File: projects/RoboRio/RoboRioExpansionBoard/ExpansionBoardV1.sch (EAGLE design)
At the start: 78 parts, among them Q1 5MHz

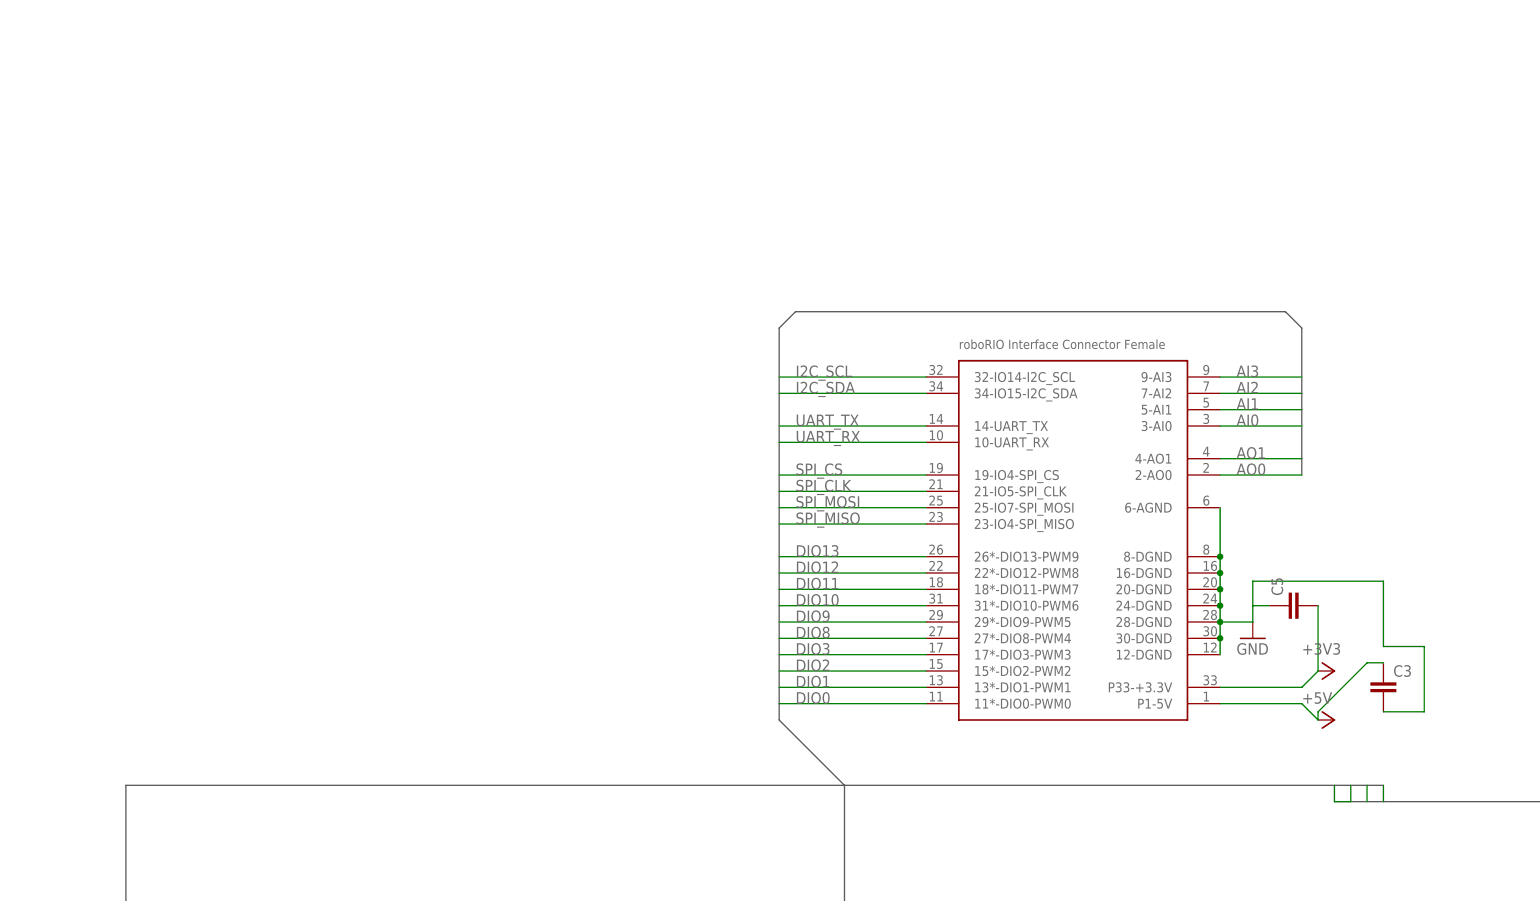
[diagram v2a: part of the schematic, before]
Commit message: AIO has been broken out
-Eric
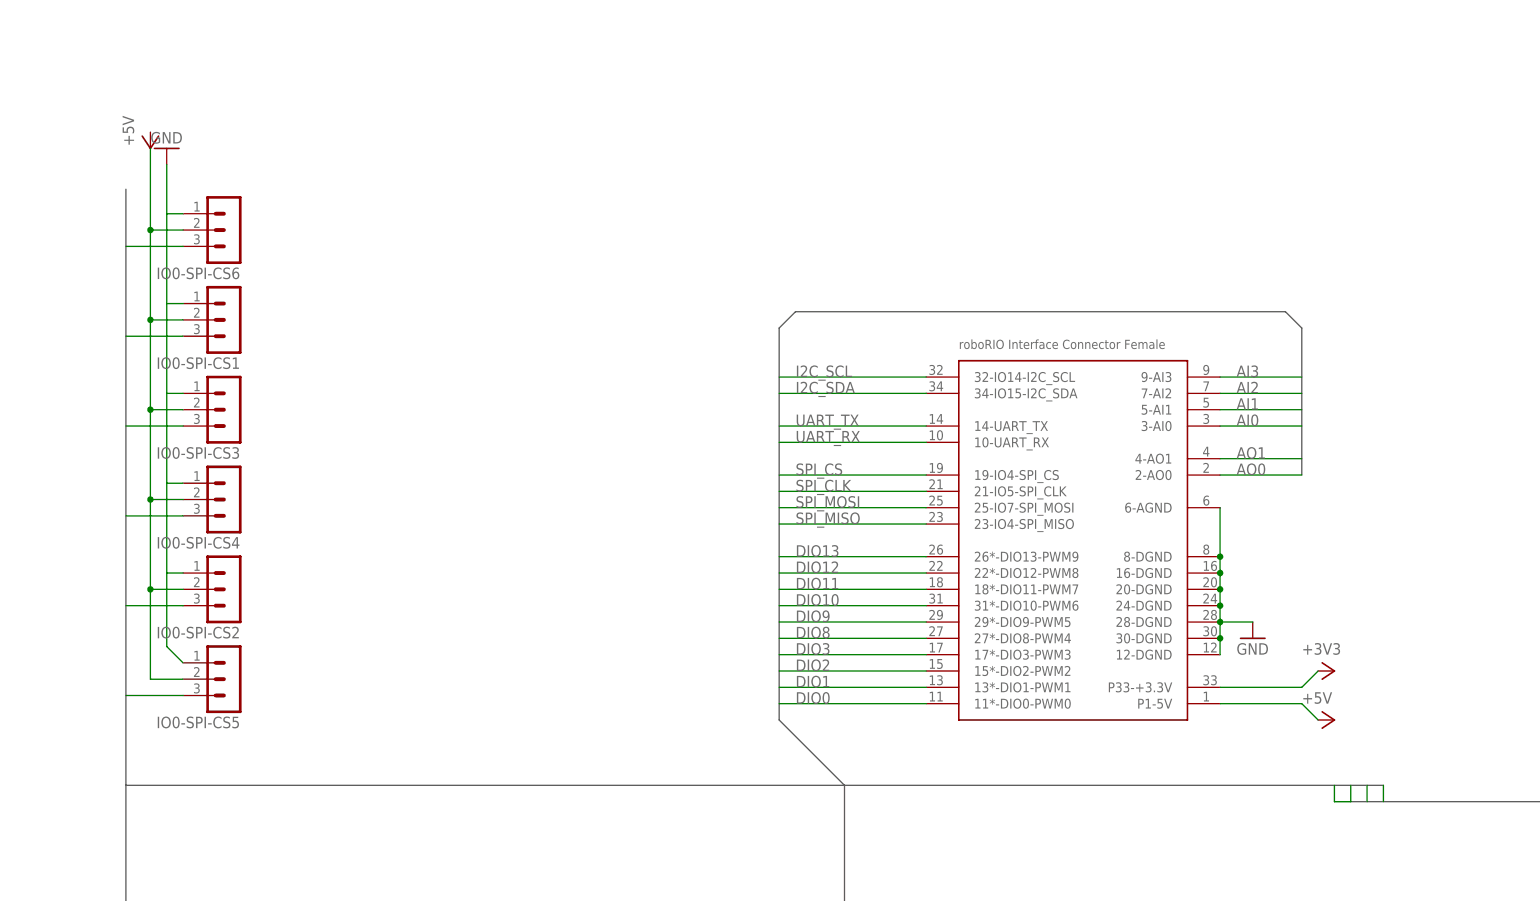
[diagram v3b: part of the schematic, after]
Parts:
- removed C3, C5: (no value), capacitor-wima:C7.5/6
- added IO0-SPI-CS1, IO0-SPI-CS2, IO0-SPI-CS3, IO0-SPI-CS4, IO0-SPI-CS5, IO0-SPI-CS6: (no value), con-lstb-modified:MA03-1
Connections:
- new net N$18: IO0-SPI-CS1.2, IO0-SPI-CS2.2, IO0-SPI-CS3.2, IO0-SPI-CS4.2, IO0-SPI-CS5.2, IO0-SPI-CS6.2
- net +3V3: no longer C5.2
- net +5V: no longer C3.1
- net AI0: now also IO0-SPI-CS6.3
- net AI1: now also IO0-SPI-CS1.3
- net AI2: now also IO0-SPI-CS3.3
- net AI3: now also IO0-SPI-CS4.3
- net AO0: now also IO0-SPI-CS2.3
- net AO1: now also IO0-SPI-CS5.3
- net GND: now also IO0-SPI-CS1.1, IO0-SPI-CS2.1, IO0-SPI-CS3.1, IO0-SPI-CS4.1, IO0-SPI-CS5.1, IO0-SPI-CS6.1; no longer C3.2, C5.1
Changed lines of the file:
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@@
 <part name="GND23" library="supply1" deviceset="GND" device=""/>
 <part name="C4" library="capacitor-wima" deviceset="C" device="7.5/6"/>
-<part name="C5" library="capacitor-wima" deviceset="C" device="7.5/6"/>
 <part name="C2" library="capacitor-wima" deviceset="C" device="7.5/6"/>
-<part name="C3" library="capacitor-wima" deviceset="C" device="7.5/6"/>
 <part name="C10" library="capacitor-wima" deviceset="C" device="7.5/6"/>
 <part name="C12" library="capacitor-wima" deviceset="C" device="7.5/6"/>
@@
 <part name="GND24" library="supply1" deviceset="GND" device=""/>
 <part name="R5" library="resistor" deviceset="R-US_" device="0309/V" value="10k"/>
+<part name="IO0-SPI-CS3" library="con-lstb-modified" deviceset="MA03-1" device=""/>
+<part name="IO0-SPI-CS4" library="con-lstb-modified" deviceset="MA03-1" device=""/>
+<part name="IO0-SPI-CS1" library="con-lstb-modified" deviceset="MA03-1" device=""/>
+<part name="IO0-SPI-CS2" library="con-lstb-modified" deviceset="MA03-1" device=""/>
+<part name="IO0-SPI-CS5" library="con-lstb-modified" deviceset="MA03-1" device=""/>
+<part name="IO0-SPI-CS6" library="con-lstb-modified" deviceset="MA03-1" device=""/>
+<part name="P+10" library="supply1" deviceset="+5V" device=""/>
+<part name="GND25" library="supply1" deviceset="GND" device=""/>
 </parts>
 <sheets>
@@
 <instance part="GND23" gate="1" x="119.38" y="152.4" rot="R90"/>
 <instance part="C4" gate="G$1" x="71.12" y="109.22" rot="R180"/>
-<instance part="C5" gate="G$1" x="-73.66" y="78.74" rot="R90"/>
 <instance part="C2" gate="G$1" x="30.48" y="114.3" rot="R90"/>
-<instance part="C3" gate="G$1" x="-58.42" y="67.31"/>
 <instance part="C10" gate="G$1" x="66.04" y="125.73" rot="R90"/>
 <instance part="C12" gate="G$1" x="-22.86" y="24.13"/>
@@
 <instance part="GND24" gate="1" x="-129.54" y="194.31" rot="R90"/>
 <instance part="R5" gate="G$1" x="-144.78" y="194.31" rot="R180"/>
+<instance part="IO0-SPI-CS3" gate="G$1" x="-237.49" y="109.22" rot="R180"/>
+<instance part="IO0-SPI-CS4" gate="G$1" x="-237.49" y="95.25" rot="R180"/>
+<instance part="IO0-SPI-CS1" gate="G$1" x="-237.49" y="123.19" rot="R180"/>
+<instance part="IO0-SPI-CS2" gate="G$1" x="-237.49" y="81.28" rot="R180"/>
+<instance part="IO0-SPI-CS5" gate="G$1" x="-237.49" y="67.31" rot="R180"/>
+<instance part="IO0-SPI-CS6" gate="G$1" x="-237.49" y="137.16" rot="R180"/>
+<instance part="P+10" gate="1" x="-250.19" y="149.86" rot="MR180"/>
+<instance part="GND25" gate="1" x="-247.65" y="149.86" rot="MR180"/>
 </instances>
 <busses>
@@
 <wire x1="-142.24" y1="50.8" x2="-254" y2="50.8" width="0.762" layer="92"/>
 <wire x1="-254" y1="50.8" x2="-254" y2="-71.12" width="0.762" layer="92"/>
+<wire x1="-254" y1="50.8" x2="-254" y2="143.51" width="0.762" layer="92"/>
 </segment>
 </bus>
@@
 <junction x="-83.82" y="76.2"/>
 <junction x="-83.82" y="73.66"/>
-<pinref part="C5" gate="G$1" pin="1"/>
-<wire x1="-78.74" y1="76.2" x2="-78.74" y2="78.74" width="0.1524" layer="91"/>
-<wire x1="-78.74" y1="78.74" x2="-76.2" y2="78.74" width="0.1524" layer="91"/>
-<wire x1="-78.74" y1="78.74" x2="-78.74" y2="82.55" width="0.1524" layer="91"/>
-<wire x1="-78.74" y1="82.55" x2="-58.42" y2="82.55" width="0.1524" layer="91"/>
-<wire x1="-58.42" y1="82.55" x2="-58.42" y2="72.39" width="0.1524" layer="91"/>
-<wire x1="-58.42" y1="72.39" x2="-52.07" y2="72.39" width="0.1524" layer="91"/>
-<pinref part="C3" gate="G$1" pin="2"/>
-<wire x1="-52.07" y1="72.39" x2="-52.07" y2="62.23" width="0.1524" layer="91"/>
-<wire x1="-52.07" y1="62.23" x2="-58.42" y2="62.23" width="0.1524" layer="91"/>
 </segment>
 <segment>
@@
 <pinref part="GND24" gate="1" pin="GND"/>
 </segment>
+<segment>
+<pinref part="GND25" gate="1" pin="GND"/>
+<pinref part="IO0-SPI-CS5" gate="G$1" pin="1"/>
+<wire x1="-247.65" y1="147.32" x2="-247.65" y2="139.7" width="0.1524" layer="91"/>
+<wire x1="-247.65" y1="139.7" x2="-247.65" y2="125.73" width="0.1524" layer="91"/>
+<wire x1="-247.65" y1="125.73" x2="-247.65" y2="111.76" width="0.1524" layer="91"/>
+<wire x1="-247.65" y1="111.76" x2="-247.65" y2="97.79" width="0.1524" layer="91"/>
+<wire x1="-247.65" y1="97.79" x2="-247.65" y2="83.82" width="0.1524" layer="91"/>
+<wire x1="-247.65" y1="83.82" x2="-247.65" y2="72.39" width="0.1524" layer="91"/>
+<wire x1="-247.65" y1="72.39" x2="-245.11" y2="69.85" width="0.1524" layer="91"/>
+<pinref part="IO0-SPI-CS6" gate="G$1" pin="1"/>
+<wire x1="-247.65" y1="139.7" x2="-245.11" y2="139.7" width="0.1524" layer="91"/>
+<pinref part="IO0-SPI-CS1" gate="G$1" pin="1"/>
+<wire x1="-247.65" y1="125.73" x2="-245.11" y2="125.73" width="0.1524" layer="91"/>
+<pinref part="IO0-SPI-CS3" gate="G$1" pin="1"/>
+<wire x1="-247.65" y1="111.76" x2="-245.11" y2="111.76" width="0.1524" layer="91"/>
+<pinref part="IO0-SPI-CS4" gate="G$1" pin="1"/>
+<wire x1="-247.65" y1="97.79" x2="-245.11" y2="97.79" width="0.1524" layer="91"/>
+<pinref part="IO0-SPI-CS2" gate="G$1" pin="1"/>
+<wire x1="-247.65" y1="83.82" x2="-245.11" y2="83.82" width="0.1524" layer="91"/>
+</segment>
 </net>
 <net name="N$1" class="0">
@@
 <wire x1="-83.82" y1="66.04" x2="-71.12" y2="66.04" width="0.1524" layer="91"/>
 <wire x1="-71.12" y1="66.04" x2="-68.58" y2="68.58" width="0.1524" layer="91"/>
-<pinref part="C5" gate="G$1" pin="2"/>
-<wire x1="-68.58" y1="68.58" x2="-68.58" y2="78.74" width="0.1524" layer="91"/>
 </segment>
 <segment>
@@
 <wire x1="-83.82" y1="63.5" x2="-71.12" y2="63.5" width="0.1524" layer="91"/>
 <wire x1="-71.12" y1="63.5" x2="-68.58" y2="60.96" width="0.1524" layer="91"/>
-<wire x1="-68.58" y1="60.96" x2="-68.58" y2="62.23" width="0.1524" layer="91"/>
-<wire x1="-68.58" y1="62.23" x2="-60.96" y2="69.85" width="0.1524" layer="91"/>
-<pinref part="C3" gate="G$1" pin="1"/>
-<wire x1="-60.96" y1="69.85" x2="-58.42" y2="69.85" width="0.1524" layer="91"/>
 </segment>
 <segment>
@@
 <label x="-78.74" y="22.86" size="1.778" layer="95"/>
 </segment>
+<segment>
+<pinref part="IO0-SPI-CS4" gate="G$1" pin="3"/>
+<wire x1="-254" y1="92.71" x2="-245.11" y2="92.71" width="0.1524" layer="91"/>
+</segment>
 </net>
 <net name="AI2" class="0">
@@
 <label x="-78.74" y="20.32" size="1.778" layer="95"/>
 </segment>
+<segment>
+<pinref part="IO0-SPI-CS3" gate="G$1" pin="3"/>
+<wire x1="-254" y1="106.68" x2="-245.11" y2="106.68" width="0.1524" layer="91"/>
+</segment>
 </net>
 <net name="AI1" class="0">
@@
 <label x="-78.74" y="17.78" size="1.778" layer="95"/>
 </segment>
+<segment>
+<pinref part="IO0-SPI-CS1" gate="G$1" pin="3"/>
+<wire x1="-254" y1="120.65" x2="-245.11" y2="120.65" width="0.1524" layer="91"/>
+</segment>
 </net>
 <net name="AI0" class="0">
@@
 <label x="-78.74" y="15.24" size="1.778" layer="95"/>
 </segment>
+<segment>
+<pinref part="IO0-SPI-CS6" gate="G$1" pin="3"/>
+<wire x1="-254" y1="134.62" x2="-245.11" y2="134.62" width="0.1524" layer="91"/>
+</segment>
 </net>
 <net name="AO1" class="0">
@@
 <label x="-78.74" y="10.16" size="1.778" layer="95"/>
 </segment>
+<segment>
+<pinref part="IO0-SPI-CS5" gate="G$1" pin="3"/>
+<wire x1="-254" y1="64.77" x2="-245.11" y2="64.77" width="0.1524" layer="91"/>
+</segment>
 </net>
 <net name="AO0" class="0">
@@
 <wire x1="-63.5" y1="7.62" x2="-81.28" y2="7.62" width="0.1524" layer="91"/>
 <label x="-78.74" y="7.62" size="1.778" layer="95"/>
+</segment>
+<segment>
+<pinref part="IO0-SPI-CS2" gate="G$1" pin="3"/>
+<wire x1="-254" y1="78.74" x2="-245.11" y2="78.74" width="0.1524" layer="91"/>
 </segment>
 </net>
@@
 </segment>
 </net>
+<net name="N$18" class="0">
+<segment>
+<wire x1="-250.19" y1="149.86" x2="-250.19" y2="137.16" width="0.1524" layer="91"/>
+<pinref part="IO0-SPI-CS5" gate="G$1" pin="2"/>
+<wire x1="-250.19" y1="137.16" x2="-250.19" y2="123.19" width="0.1524" layer="91"/>
+<wire x1="-250.19" y1="123.19" x2="-250.19" y2="109.22" width="0.1524" layer="91"/>
+<wire x1="-250.19" y1="109.22" x2="-250.19" y2="95.25" width="0.1524" layer="91"/>
+<wire x1="-250.19" y1="95.25" x2="-250.19" y2="81.28" width="0.1524" layer="91"/>
+<wire x1="-250.19" y1="81.28" x2="-250.19" y2="67.31" width="0.1524" layer="91"/>
+<wire x1="-250.19" y1="67.31" x2="-245.11" y2="67.31" width="0.1524" layer="91"/>
+<junction x="-250.19" y="81.28"/>
+<junction x="-250.19" y="95.25"/>
+<junction x="-250.19" y="137.16"/>
+<pinref part="IO0-SPI-CS6" gate="G$1" pin="2"/>
+<wire x1="-250.19" y1="137.16" x2="-245.11" y2="137.16" width="0.1524" layer="91"/>
+<junction x="-250.19" y="123.19"/>
+<pinref part="IO0-SPI-CS1" gate="G$1" pin="2"/>
+<wire x1="-250.19" y1="123.19" x2="-245.11" y2="123.19" width="0.1524" layer="91"/>
+<pinref part="IO0-SPI-CS4" gate="G$1" pin="2"/>
+<wire x1="-250.19" y1="95.25" x2="-245.11" y2="95.25" width="0.1524" layer="91"/>
+<pinref part="IO0-SPI-CS2" gate="G$1" pin="2"/>
+<wire x1="-250.19" y1="81.28" x2="-245.11" y2="81.28" width="0.1524" layer="91"/>
+<junction x="-250.19" y="109.22"/>
+<pinref part="IO0-SPI-CS3" gate="G$1" pin="2"/>
+<wire x1="-250.19" y1="109.22" x2="-245.11" y2="109.22" width="0.1524" layer="91"/>
+</segment>
+</net>

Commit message: Added some connections to the ADC
-eric
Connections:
- net IO12: now also ADC./CS
- net IO13: now also ADC.DIN
- net IO14: now also ADC.DOUT
- net IO15: now also ADC.CLK
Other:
- note added: "Change AAAALLL of these to 4 pins. Library is already there?"
- moved on the sheet: ADC, ADC0, ADC1, ADC2, ADC3, ADC4, ADC5, ADC6, ADC7, C10, C4

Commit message: Moved the PWM breakouts
to show its only connected to the roborio,
eric
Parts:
- removed RRDIO0, RRDIO1, RRDIO10, RRDIO11, RRDIO12, RRDIO13, RRDIO2, RRDIO3, RRDIO8, RRDIO9: (no value), con-lstb-modified:MA03-1
- added PWM0, PWM1, PWM2, PWM3, PWM4, PWM5, PWM6, PWM7, PWM8, PWM9: (no value), con-lstb-modified:MA03-1
- renumbered IO0-SPI-CS1 to AI1, IO0-SPI-CS2 to AI4, IO0-SPI-CS3 to AI2, IO0-SPI-CS4 to AI3, IO0-SPI-CS5 to AI5, IO0-SPI-CS6 to AIO
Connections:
- net +5V: now also PWM0.2, PWM1.2, PWM2.2, PWM3.2, PWM4.2, PWM5.2, PWM6.2, PWM7.2, PWM8.2, PWM9.2; no longer RRDIO0.2, RRDIO1.2, RRDIO10.2, RRDIO11.2, RRDIO12.2, RRDIO13.2, RRDIO2.2, RRDIO3.2, RRDIO8.2, RRDIO9.2
- net DIO0: now also PWM0.1; no longer RRDIO0.1
- net DIO1: now also PWM1.1; no longer RRDIO1.1
- net DIO10: now also PWM6.1; no longer RRDIO10.1
- net DIO11: now also PWM7.1; no longer RRDIO11.1
- net DIO12: now also PWM8.1; no longer RRDIO12.1
- net DIO13: now also PWM9.1; no longer RRDIO13.1
- net DIO2: now also PWM2.1; no longer RRDIO2.1
- net DIO3: now also PWM3.1; no longer RRDIO3.1
- net DIO8: now also PWM4.1; no longer RRDIO8.1
- net DIO9: now also PWM5.1; no longer RRDIO9.1
- net GND: now also PWM0.3, PWM1.3, PWM2.3, PWM3.3, PWM4.3, PWM5.3, PWM6.3, PWM7.3, PWM8.3, PWM9.3; no longer RRDIO0.3, RRDIO1.3, RRDIO10.3, RRDIO11.3, RRDIO12.3, RRDIO13.3, RRDIO2.3, RRDIO3.3, RRDIO8.3, RRDIO9.3
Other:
- note added: "POWER LED"
- moved on the sheet: GREEN1, R5

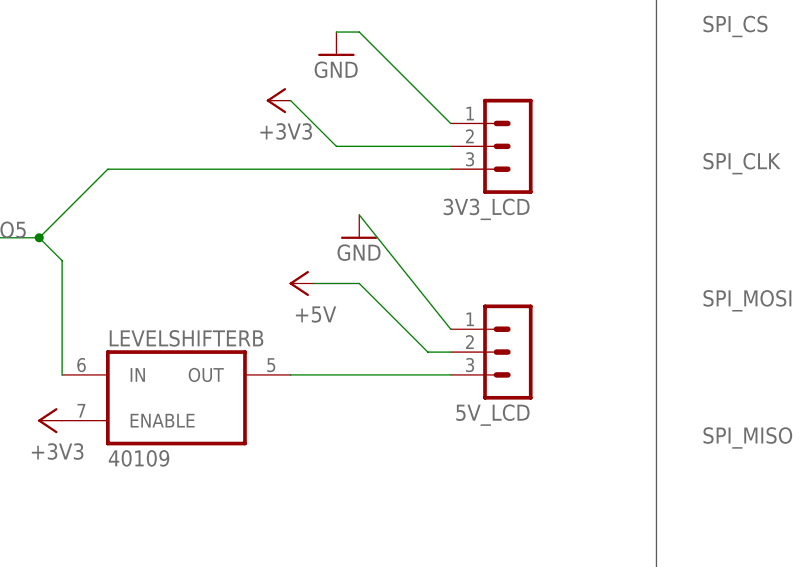
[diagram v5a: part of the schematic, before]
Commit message: Made connections prettier
to better understand it.
eric
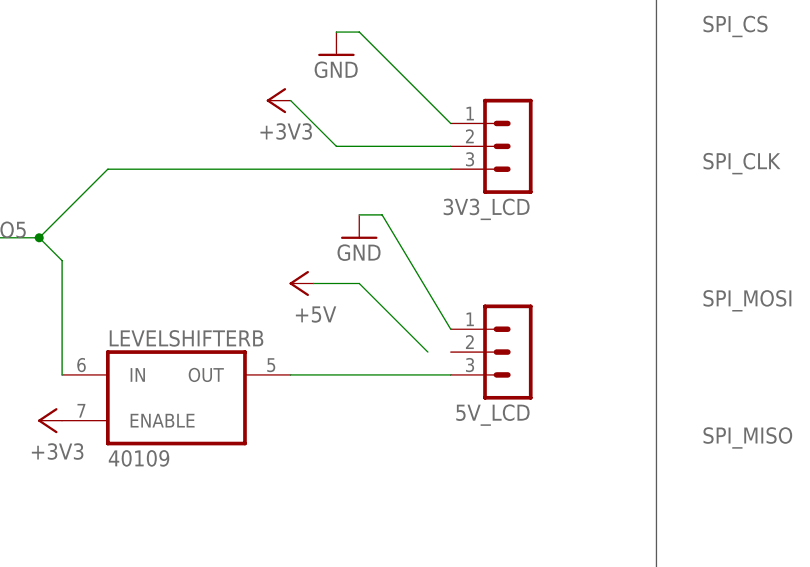
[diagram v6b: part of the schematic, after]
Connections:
- net +5V: no longer 5V_LCD.2
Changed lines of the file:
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@@
-</segment>
-<segment>
-<pinref part="5V_LCD" gate="G$1" pin="1"/>
-<wire x1="58.42" y1="-22.86" x2="48.26" y2="-10.16" width="0.1524" layer="91"/>
-<pinref part="GND22" gate="1" pin="GND"/>
 </segment>
 <segment>
@@
 <pinref part="AI4" gate="G$1" pin="1"/>
 <wire x1="-247.65" y1="83.82" x2="-245.11" y2="83.82" width="0.1524" layer="91"/>
+</segment>
+<segment>
+<pinref part="5V_LCD" gate="G$1" pin="1"/>
+<wire x1="58.42" y1="-22.86" x2="50.8" y2="-10.16" width="0.1524" layer="91"/>
+<pinref part="GND22" gate="1" pin="GND"/>
+<wire x1="50.8" y1="-10.16" x2="48.26" y2="-10.16" width="0.1524" layer="91"/>
 </segment>
 </net>
@@
 </segment>
 <segment>
-<pinref part="5V_LCD" gate="G$1" pin="2"/>
-<wire x1="58.42" y1="-25.4" x2="55.88" y2="-25.4" width="0.1524" layer="91"/>
 <pinref part="P+9" gate="1" pin="+5V"/>
 <wire x1="55.88" y1="-25.4" x2="48.26" y2="-17.78" width="0.1524" layer="91"/>

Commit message: Tidied up connections
eric
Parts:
- removed C10: (no value), capacitor-wima:C7.5/6
- added C1: .1uF, capacitor-wima:C7.5/6
- C12: value (none) -> .1 uF
- C13, C2, C4: value (none) -> .1uF
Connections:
- net +3V3: now also C1.2; no longer ADC.VDD, C4.1
- net +5V: now also 5V_LCD.2, ADC.VDD, C4.1; no longer C10.1
- net GND: now also C1.1; no longer C10.2
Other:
- note added: "test"
- moved on the sheet: C12, C13

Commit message: Updated PWM pass-throughs to be a separate bus
also removed 3.3v connection for LCD so there is only one
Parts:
- removed 3V3_LCD: (no value), con-lstb-modified:MA03-1
- R5: value 10k -> 150
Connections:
- net DIO0 renamed PWM0
- net DIO1 renamed PWM1
- net DIO10 renamed PWM6
- net DIO11 renamed PWM7
- net DIO12 renamed PWM8
- net DIO13 renamed PWM9
- net DIO2 renamed PWM2
- net DIO3 renamed PWM3
- net DIO9 renamed PWM5
- removed net DIO8: PWM4.1, U$1.27*-DIO8-PWM4, U$2.27*-IO8-PWM4
- removed net N$15: 5V_LCD.3, LEVELSHIFTERB.OUT
- removed net N$16: C13.2
- removed net N$18: AI1.2, AI2.2, AI3.2, AI4.2, AI5.2, AIO.2
- new net PWM4: U$1.27*-DIO8-PWM4, U$2.27*-IO8-PWM4
- net +3V3: no longer 3V3_LCD.2, LEVELSHIFTERB.ENABLE
- net +5V: now also AI1.2, AI2.2, AI3.2, AI4.2, AI5.2, AIO.2
- net GND: now also ADC./CS, C13.2; no longer 3V3_LCD.1
- net IO12: no longer ADC./CS
- net IO5: now also 5V_LCD.3; no longer 3V3_LCD.3, LEVELSHIFTERB.IN
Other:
- moved on the sheet: 5V_LCD, AI1, AI2, AI3, AI4, AI5, AIO, C13, GREEN1, LEVELSHIFTERB, R5
